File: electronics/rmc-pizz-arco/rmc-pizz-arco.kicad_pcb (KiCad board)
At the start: 4 copper layers, 88 x 112 mm, 117 parts, among them J1 PZT, J2 PZT, J3 PZT, J4 PZT, J5 PZT, J6 PZT, J7 DIN-8, J8 PIZZ/ARCO, J9 12V DC, U1 OPA2191, U2 OPA2191, U3 OPA2191, U4 OPA2191, U5 OPA2191, U6 OPA2191, U7 OPA2191, U8 CD4066B, U9 CD4066B

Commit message: Fixed errors and wrote up notes
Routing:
- net AGND: track 102.2 -> 99.0 mm
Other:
- board text added: "12 V DC FLOATING SUPPLY ONLY"
- board text added: "RMC pizz/arco 6 channel rev A"
- board text removed: "12V DC FLOATING SUPPLY ONLY"
- board text removed: "RMC pizz/arco 6ch rev A"

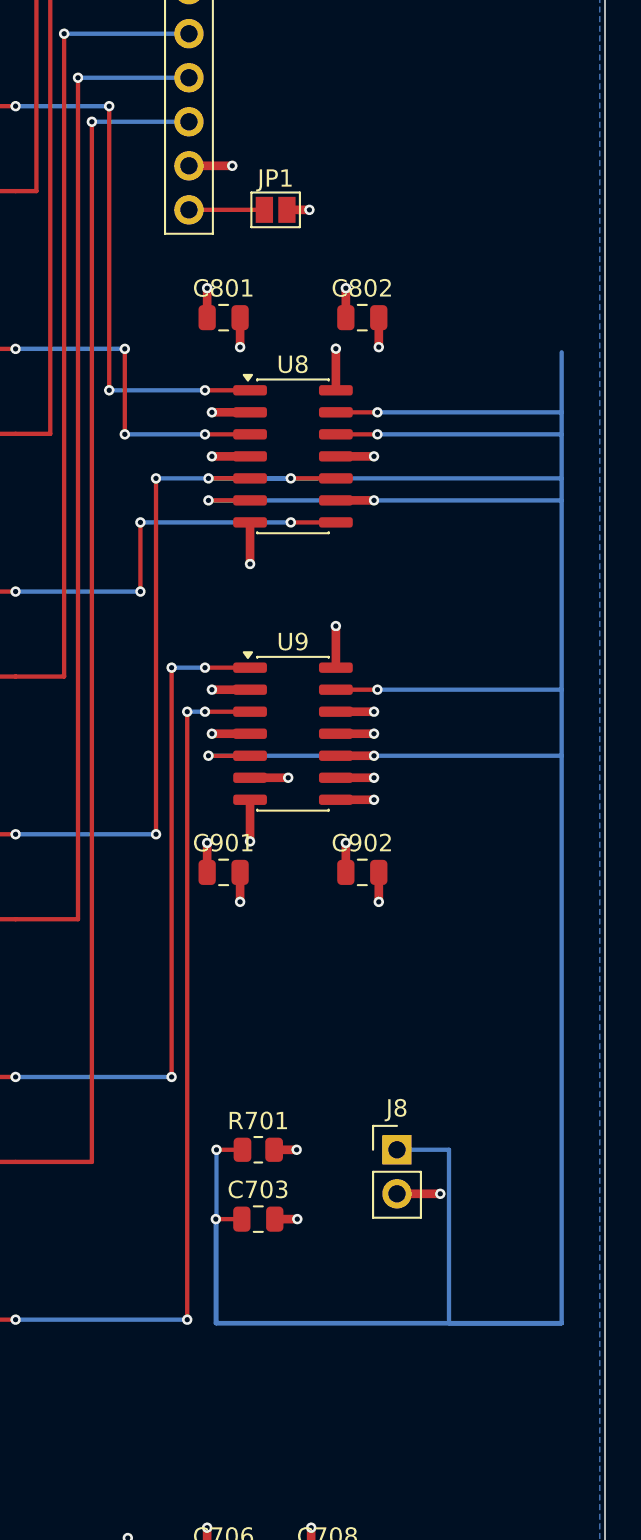
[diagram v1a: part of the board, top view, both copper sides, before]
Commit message: Fixed errors and wrote up pcbway order
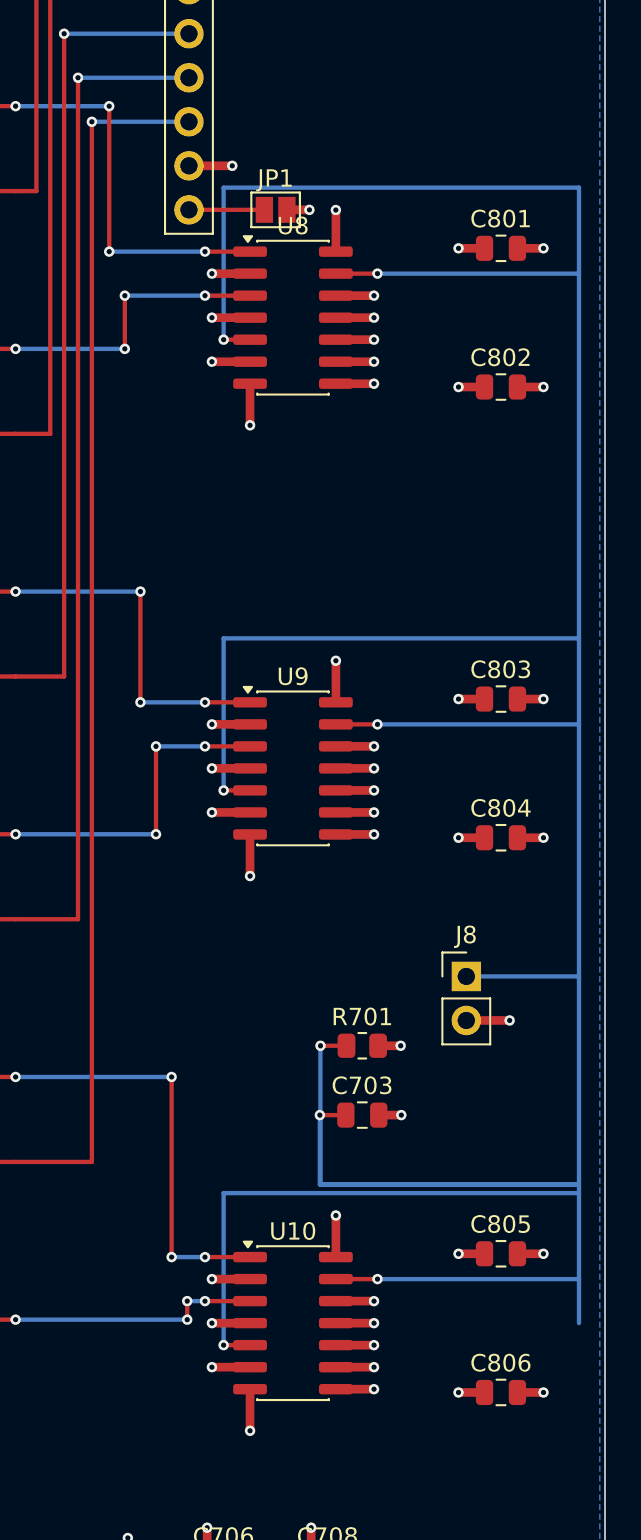
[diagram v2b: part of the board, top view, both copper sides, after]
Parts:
- removed C901, C902: 100n, C_0805_2012Metric
- added C803: 100n, C_0805_2012Metric, F.Cu at (82.0, 48.0)
- added C804: 100n, C_0805_2012Metric, F.Cu at (82.0, 56.0)
- added C805: 100n, C_0805_2012Metric, F.Cu at (82.0, 80.0)
- added C806: 100n, C_0805_2012Metric, F.Cu at (82.0, 88.0)
- added U10: CD4066B, SO-14_3.9x8.65mm_P1.27mm, F.Cu at (70.0, 84.0)
- moved C801 16.5 mm to (82.0, 22.0)
- moved J8 10.8 mm to (80.0, 64.0)
- moved C802 8.94 mm to (82.0, 30.0)
- moved C703 8.49 mm to (74.0, 72.0)
- moved R701 8.49 mm to (74.0, 68.0)
- moved U8 8.00 mm to (70.0, 26.0)
- moved U9 2.00 mm to (70.0, 52.0)
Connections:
- U8 pad 10: SWN4 -> AGND
- U8 pad 12: SW_CTL -> V-
- U8 pad 6: SW_CTL -> V-
- U8 pad 8: SWN3 -> AGND
- U9 pad 1: SWN5 -> SWN3
- U9 pad 3: SWN6 -> SWN4
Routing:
- net SWN6: track 79.4 -> 45.4 mm
- net SWN4: track 69.8 -> 49.4 mm
- net AGND: track 99.0 -> 118.8 mm, vias 59 -> 69
- net SWN5: track 68.0 -> 54.7 mm
- net V-: track 60.0 -> 72.3 mm, vias 24 -> 30
- net SW_CTL: track 241.8 -> 251.3 mm
- net SWN1: track 60.7 -> 52.7 mm
- net V+: track 43.7 -> 47.2 mm, vias 19 -> 21
- net SWN3: track 53.3 -> 50.7 mm
- net SWN2: track 49.3 -> 47.4 mm

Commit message: Made the assets accessible as a KiCad project
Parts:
- C101, C102, C103, C104, C105, C106, C107, C201, C202, C203, C204, C205, C206, C207, C301, C302, C303, C304, C305, C306, C307, C401, C402, C403, C404, C405, C406, C407, C501, C502, C503, C504, C505, C506, C507, C601, C602, C603, C604, C605, C606, C607, C702, C703, C704, C705, C706, C707, C708, C709, C801, C802, C803, C804, C805, C806: footprint C_0805_2012Metric -> Capacitor_SMD:C_0805_2012Metric
- C701: footprint CP_Elec_6.3x5.4 -> Capacitor_SMD:CP_Elec_6.3x5.4
- D701: footprint D_SOD-123 -> Diode_SMD:D_SOD-123
- D702: footprint D_SMA -> Diode_SMD:D_SMA
- F701: footprint Fuse_1206_3216Metric -> Fuse:Fuse_1206_3216Metric
- J1, J2, J3, J4, J5, J6: footprint PinHeader_1x03_P2.54mm_Vertical -> Connector_PinHeader_2.54mm:PinHeader_1x03_P2.54mm_Vertical
- J7: footprint PinHeader_1x08_P2.54mm_Vertical -> Connector_PinHeader_2.54mm:PinHeader_1x08_P2.54mm_Vertical
- J8, J9: footprint PinHeader_1x02_P2.54mm_Vertical -> Connector_PinHeader_2.54mm:PinHeader_1x02_P2.54mm_Vertical
- JP1: footprint SolderJumper-2_P1.3mm_Open_Pad1.0x1.5mm -> Jumper:SolderJumper-2_P1.3mm_Open_Pad1.0x1.5mm
- R101, R102, R103, R104, R105, R106, R201, R202, R203, R204, R205, R206, R301, R302, R303, R304, R305, R306, R401, R402, R403, R404, R405, R406, R501, R502, R503, R504, R505, R506, R601, R602, R603, R604, R605, R606, R701, R702, R703, R704: footprint R_0805_2012Metric -> Resistor_SMD:R_0805_2012Metric
- U1, U2, U3, U4, U5, U6, U7: footprint SOIC-8_3.9x4.9mm_P1.27mm -> Package_SO:SOIC-8_3.9x4.9mm_P1.27mm
- U10, U8, U9: footprint SO-14_3.9x8.65mm_P1.27mm -> Package_SO:SO-14_3.9x8.65mm_P1.27mm

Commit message: We believe this system can be safely run at 9v DC. We now check for KiCad installation and fail if not found. We updated docs on what happens if the power supply fails.
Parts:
- J9: value 12V DC -> 9-15V DC
- R702, R703: value 10k -> 100k
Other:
- board text added: "FLOATING SUPPLY ONLY 9-15V DC"
- board text removed: "12 V DC FLOATING SUPPLY ONLY"

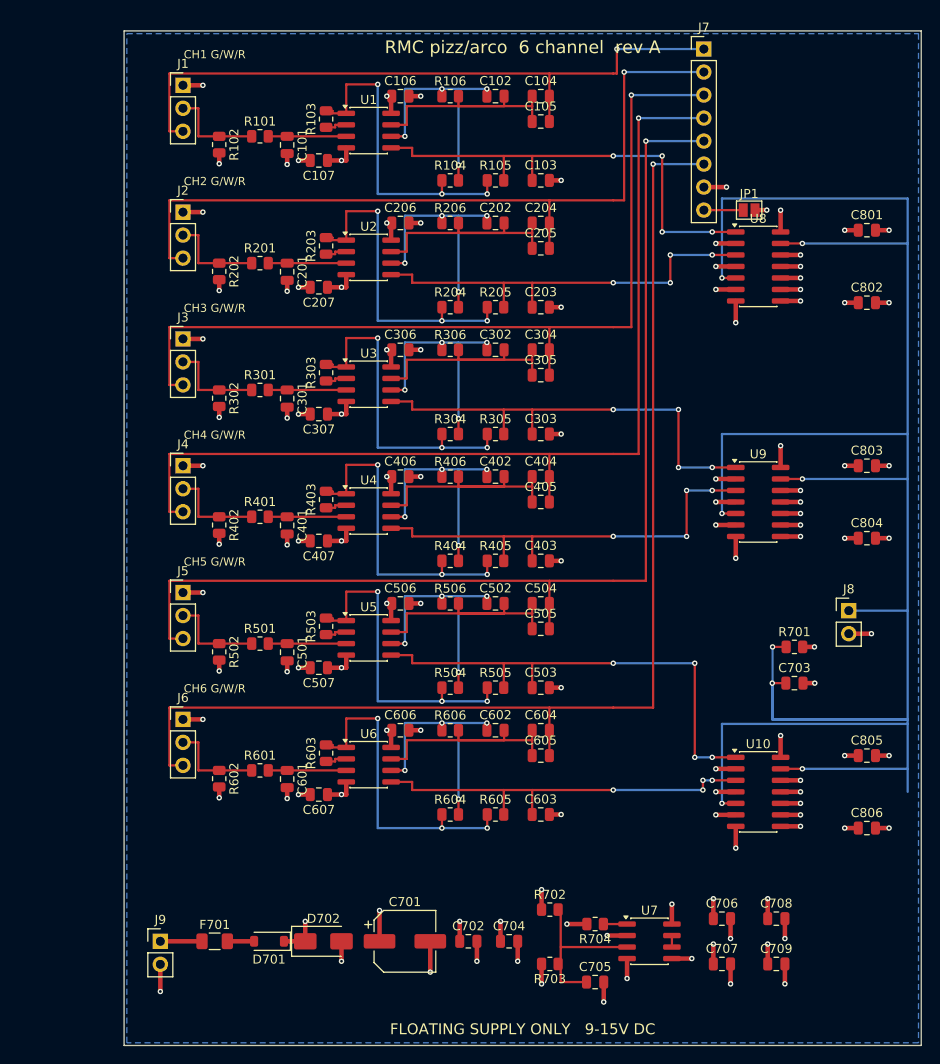
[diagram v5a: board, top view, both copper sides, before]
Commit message: Supersede: bipolar +/-9V charge-pump board with onboard battery
Complete and self-consistent -- verify.py matches the schematic to design.py exactly (58 nets, 322 pin connections) and the board lays out at 56 x 94 mm with DRC nearly clean. Kept as a record of the +/-9V exploration only.

Superseded by RMC's reply of 2026-07-30: the board takes bipolar power from the Poly-Drive II over DIN-8 pins 7 and 8 with the shell as ground, so there is no battery, no charge pump and no power section. See electronics/STATE.md.
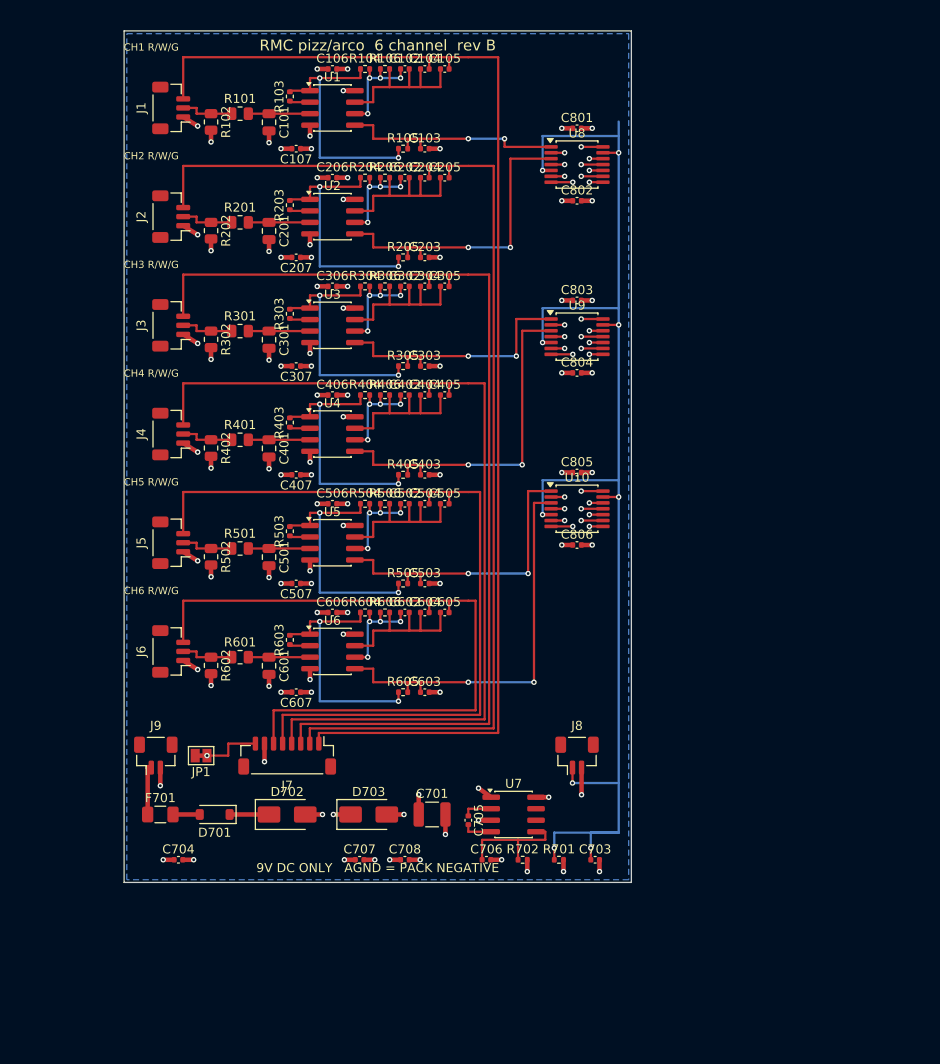
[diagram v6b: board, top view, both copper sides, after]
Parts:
- removed C702: 10u, Capacitor_SMD:C_0805_2012Metric
- removed C709: 100n, Capacitor_SMD:C_0805_2012Metric
- removed R703: 100k, Resistor_SMD:R_0805_2012Metric
- removed R704: 10R, Resistor_SMD:R_0805_2012Metric
- added D703: SMAJ10A, Diode_SMD:D_SMA, F.Cu at (27.0, 86.5)
- C102, C103, C104, C105, C106, C107, C202, C203, C204, C205, C206, C207, C302, C303, C304, C305, C306, C307, C402, C403, C404, C405, C406, C407, C502, C503, C504, C505, C506, C507, C602, C603, C604, C605, C606, C607, C703, C704, C705, C706, C707, C708, C801, C802, C803, C804, C805, C806: footprint Capacitor_SMD:C_0805_2012Metric -> Capacitor_SMD:C_0402_1005Metric
- C701: value 100u/25V -> 22u/16V; footprint Capacitor_SMD:CP_Elec_6.3x5.4 -> Capacitor_SMD:C_1210_3225Metric
- D702: value SMAJ15A -> SMAJ10A
- J1, J2, J3, J4, J5, J6: footprint Connector_PinHeader_2.54mm:PinHeader_1x03_P2.54mm_Vertical -> Connector_JST:JST_SH_BM03B-SRSS-TB_1x03-1MP_P1.00mm_Vertical
- J7: footprint Connector_PinHeader_2.54mm:PinHeader_1x08_P2.54mm_Vertical -> Connector_JST:JST_SH_BM08B-SRSS-TB_1x08-1MP_P1.00mm_Vertical
- J8: footprint Connector_PinHeader_2.54mm:PinHeader_1x02_P2.54mm_Vertical -> Connector_JST:JST_SH_BM02B-SRSS-TB_1x02-1MP_P1.00mm_Vertical
- J9: value 9-15V DC -> 9V DC ONLY; footprint Connector_PinHeader_2.54mm:PinHeader_1x02_P2.54mm_Vertical -> Connector_JST:JST_SH_BM02B-SRSS-TB_1x02-1MP_P1.00mm_Vertical
- R103, R104, R105, R106, R203, R204, R205, R206, R303, R304, R305, R306, R403, R404, R405, R406, R503, R504, R505, R506, R603, R604, R605, R606, R701: footprint Resistor_SMD:R_0805_2012Metric -> Resistor_SMD:R_0402_1005Metric
- R702: value 100k -> 10R; footprint Resistor_SMD:R_0805_2012Metric -> Resistor_SMD:R_0402_1005Metric
- U10, U8, U9: footprint Package_SO:SO-14_3.9x8.65mm_P1.27mm -> Package_SO:TSSOP-14_4.4x5mm_P0.65mm
- U7: value OPA2191 -> TC1044S
- moved J7 90.6 mm to (18.0, 80.0), turned to 180 degrees
- moved JP1 85.4 mm to (8.50, 80.0), turned to 180 degrees
- moved C805 44.7 mm to (50.0, 48.8)
- moved C806 44.7 mm to (50.0, 56.8)
- moved C707 41.6 mm to (26.0, 91.5)
- moved C708 41.5 mm to (31.0, 91.5)
- moved C704 37.6 mm to (6.00, 91.5)
- moved U10 37.1 mm to (50.0, 52.8)
- moved C803 36.8 mm to (50.0, 29.8)
- moved C804 36.8 mm to (50.0, 37.8)
- moved R701 35.0 mm to (48.0, 91.5)
- moved J8 34.0 mm to (50.0, 80.0)
- moved C801 33.9 mm to (50.0, 10.8)
- moved C802 33.9 mm to (50.0, 18.8)
- moved C703 29.4 mm to (52.0, 91.5)
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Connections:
- C701 pad 2: V- -> AGND
- C704 pad 2: V- -> AGND
- C705 pad 1: MIDREF -> CPFLY_P
- C705 pad 2: V- -> CPFLY_N
- C706 pad 1: AGND -> CPOUT
- C706 pad 2: V+ -> AGND
- C707 pad 1: AGND -> V-
- C707 pad 2: V- -> AGND
- C708 pad 1: V+ -> V-
- D702 pad 2: V- -> AGND
- J9 pad 2: V- -> AGND
- R702 pad 1: V+ -> CPOUT
- R702 pad 2: MIDREF -> V-
- U7 pad 1: AGND_DRV -> V+
- U7 pad 2: AGND -> CPFLY_P
- U7 pad 3: MIDREF -> AGND
- U7 pad 4: V- -> CPFLY_N
- U7 pad 5: AGND -> CPOUT
- U7 pad 6: SPARE -> (no net)
- U7 pad 7: SPARE -> (no net)
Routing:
- net SW_CTL: track 251.3 -> 146.1 mm, vias 8 -> 9
- net OUT1: track 74.9 -> 137.6 mm, vias 1 -> 0
- net OUT6: track 132.2 -> 77.6 mm, vias 1 -> 0
- net OUT2: track 86.3 -> 125.5 mm, vias 1 -> 0
- net OUT5: track 120.7 -> 89.6 mm, vias 1 -> 0
- net V-: track 72.3 -> 42.4 mm
- net SWN1: track 52.7 -> 26.3 mm, vias 4 -> 2
- net SWN3: track 50.7 -> 29.5 mm, vias 4 -> 2
- net SWN5: track 54.7 -> 34.5 mm, vias 4 -> 2
- net MIDREF: track 18.7 -> 0.00 mm
- net OUT3: track 97.8 -> 113.5 mm, vias 1 -> 0
- net APN3: track 27.5 -> 12.0 mm
- net APN5: track 27.5 -> 12.0 mm
- net APN4: track 27.5 -> 12.0 mm
- net APN2: track 27.5 -> 12.0 mm
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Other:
- board size 88 x 112 mm -> 56 x 94 mm
- board text added: "9V DC ONLY AGND = PACK NEGATIVE"
- board text added: "CH1 R/W/G"
- board text added: "CH2 R/W/G"
- board text added: "CH3 R/W/G"
- board text added: "CH4 R/W/G"
- board text added: "CH5 R/W/G"
- board text added: "CH6 R/W/G"
- board text added: "RMC pizz/arco 6 channel rev B"
- board text removed: "CH1 G/W/R"
- board text removed: "CH2 G/W/R"
- board text removed: "CH3 G/W/R"
- board text removed: "CH4 G/W/R"
- board text removed: "CH5 G/W/R"
- board text removed: "CH6 G/W/R"
- board text removed: "FLOATING SUPPLY ONLY 9-15V DC"
- board text removed: "RMC pizz/arco 6 channel rev A"
